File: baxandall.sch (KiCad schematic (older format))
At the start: 17 parts, among them P1 CONN_01X04, P3 CONN_01X03, U1 OP275

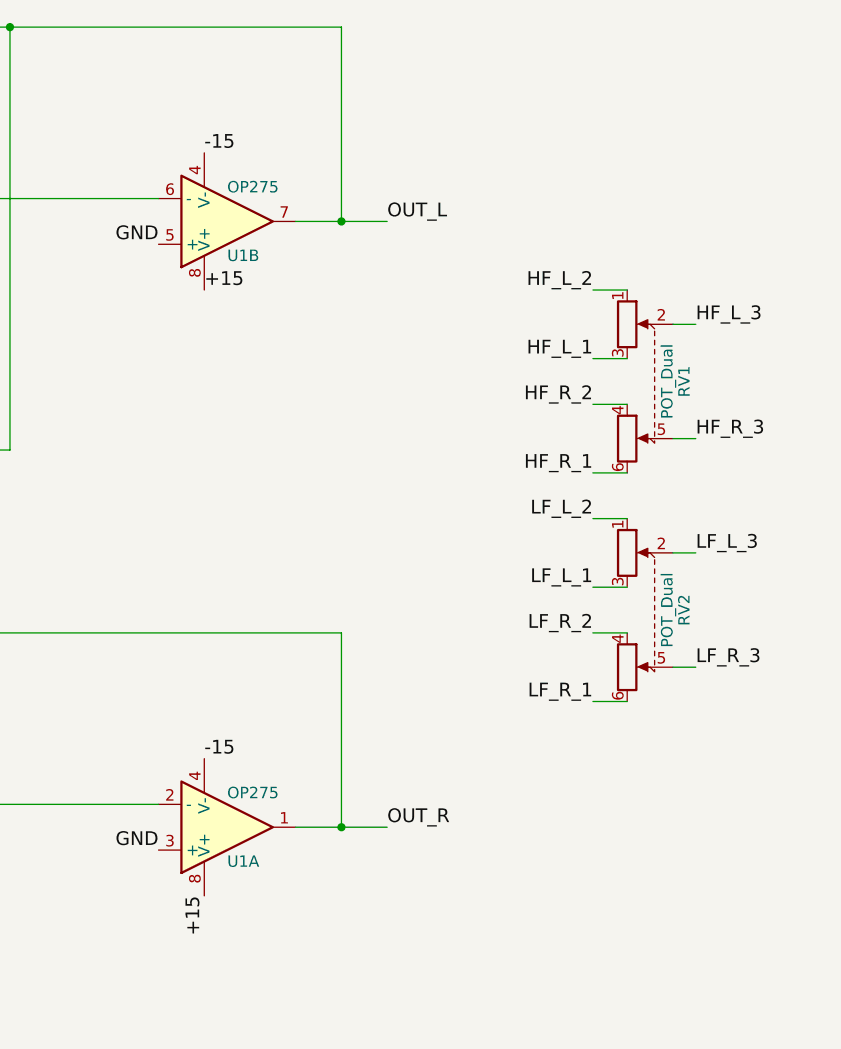
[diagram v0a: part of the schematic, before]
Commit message: Update potentiometers properties
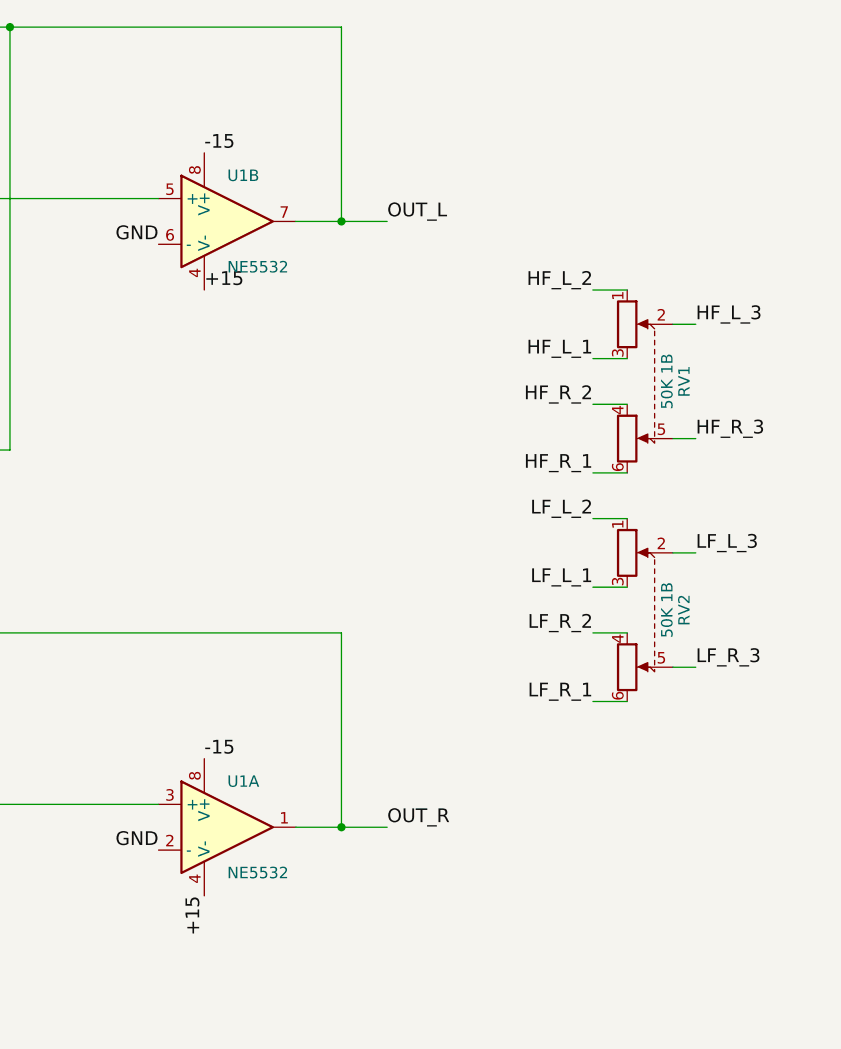
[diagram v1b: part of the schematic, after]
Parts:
- removed U1: OP275, Housings_DIP:DIP-8_W7.62mm_LongPads, symbol OP275
- added U1: NE5532, Housings_DIP:DIP-8_W7.62mm_LongPads, symbol NE5532
- RV1, RV2: value POT_Dual -> 50K 1B; Description (none) -> Potentiomètres 50 KOhms 20%; Distributor (none) -> Mouser; Distributor Part # (none) -> 688-RK09L122002M; Manufacturer (none) -> ALPS; Mfg_Part_# (none) -> RK09L122002M
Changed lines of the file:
@@
 LIBS:contrib
 LIBS:valves
+LIBS:baxandall-cache
 EELAYER 25 0
 EELAYER END
@@
 	1    3800 6350
 	0    1    1    0
-$EndComp
-$Comp
-L OP275 U1
-U 1 1 56A0BD66
-P 5050 5350
-F 0 "U1" H 5050 5500 50  0000 L CNN
-F 1 "OP275" H 5050 5200 50  0000 L CNN
-F 2 "Housings_DIP:DIP-8_W7.62mm_LongPads" H 4950 5400 50  0001 C CNN
-F 3 "" H 5050 5500 50  0000 C CNN
-	1    5050 5350
-	1    0    0    1
 $EndComp
 $Comp
@@
 Text Label 7150 1050 2    60   ~ 0
 GND
-$Comp
-L OP275 U1
-U 2 1 56AA63D5
-P 5050 2700
-F 0 "U1" H 5050 2850 50  0000 L CNN
-F 1 "OP275" H 5050 2550 50  0000 L CNN
-F 2 "Housings_DIP:DIP-8_W7.62mm_LongPads" H 4950 2750 50  0001 C CNN
-F 3 "" H 5050 2850 50  0000 C CNN
-	2    5050 2700
-	1    0    0    1
-$EndComp
 Text Label 4950 3000 0    60   ~ 0
 +15
@@
 P 6900 3400
 F 0 "RV1" H 6900 3550 50  0000 C CNN
-F 1 "POT_Dual" H 6900 3475 50  0000 C CNN
+F 1 "50K 1B" H 6900 3475 50  0000 C CNN
 F 2 "" H 7150 3325 50  0001 C CNN
-F 3 "" H 7150 3325 50  0001 C CNN
+F 3 "http://www.alps.com/prod/info/E/HTML/Potentiometer/RotaryPotentiometers/RK09L/RK09L122002M.html" H 7150 3325 50  0001 C CNN
+F 4 "RK09L122002M" H 6900 3400 60  0001 C CNN "Mfg_Part_#"
+F 5 "Mouser" H 6900 3400 60  0001 C CNN "Distributor"
+F 6 "688-RK09L122002M" H 6900 3400 60  0001 C CNN "Distributor Part #"
+F 7 "Potentiomètres 50 KOhms 20%" H 6900 3400 60  0001 C CNN "Description"
+F 8 "ALPS" H 6900 3400 60  0001 C CNN "Manufacturer"
 	1    6900 3400
 	0    1    1    0
@@
 Wire Wire Line
 	6650 3800 6800 3800
+Wire Wire Line
+	6650 4800 6800 4800
+Wire Wire Line
+	6800 4500 6650 4500
+Wire Wire Line
+	6650 4300 6800 4300
+Wire Wire Line
+	6800 4000 6650 4000
+Wire Wire Line
+	7000 4150 7100 4150
+Wire Wire Line
+	7100 4650 7000 4650
+$Comp
+L NE5532 U1
+U 2 1 5A0DA73B
+P 5050 2700
+F 0 "U1" H 5050 2900 50  0000 L CNN
+F 1 "NE5532" H 5050 2500 50  0000 L CNN
+F 2 "Housings_DIP:DIP-8_W7.62mm_LongPads" H 5050 2700 50  0001 C CNN
+F 3 "http://www.ti.com/lit/gpn/ne5532" H 5050 2700 50  0001 C CNN
+F 4 "NE5532P" H 5050 2700 60  0001 C CNN "Mfg_Part_#"
+F 5 "Mouser" H 5050 2700 60  0001 C CNN "Distributor"
+F 6 "595-NE5532P" H 5050 2700 60  0001 C CNN "Distributor Part #"
+F 7 "8-PDIP" H 5050 2700 60  0001 C CNN "Package"
+F 8 "Amplificateurs opérationnels - Amplis-Op Dual Low Noise" H 5050 2700 60  0001 C CNN "Description"
+F 9 "Texas Instruments" H 5050 2700 60  0001 C CNN "Manufacturer"
+	2    5050 2700
+	1    0    0    -1
+$EndComp
+$Comp
+L NE5532 U1
+U 1 1 5A0DAB29
+P 5050 5350
+F 0 "U1" H 5050 5550 50  0000 L CNN
+F 1 "NE5532" H 5050 5150 50  0000 L CNN
+F 2 "Housings_DIP:DIP-8_W7.62mm_LongPads" H 5050 5350 50  0001 C CNN
+F 3 "http://www.ti.com/lit/gpn/ne5532" H 5050 5350 50  0001 C CNN
+F 4 "NE5532P" H 5050 5350 60  0001 C CNN "Mfg_Part_#"
+F 5 "Mouser" H 5050 5350 60  0001 C CNN "Distributor"
+F 6 "595-NE5532P" H 5050 5350 60  0001 C CNN "Distributor Part #"
+F 7 "8-PDIP" H 5050 5350 60  0001 C CNN "Package"
+F 8 "Amplificateurs opérationnels - Amplis-Op Dual Low Noise" H 5050 5350 60  0001 C CNN "Description"
+F 9 "Texas Instruments" H 5050 5350 60  0001 C CNN "Manufacturer"
+	1    5050 5350
+	1    0    0    -1
+$EndComp
 $Comp
 L POT_Dual RV2
-U 1 1 5A0C7786
+U 1 1 5A0DB04F
 P 6900 4400
 F 0 "RV2" H 6900 4550 50  0000 C CNN
-F 1 "POT_Dual" H 6900 4475 50  0000 C CNN
+F 1 "50K 1B" H 6900 4475 50  0000 C CNN
 F 2 "" H 7150 4325 50  0001 C CNN
-F 3 "" H 7150 4325 50  0001 C CNN
+F 3 "http://www.alps.com/prod/info/E/HTML/Potentiometer/RotaryPotentiometers/RK09L/RK09L122002M.html" H 7150 4325 50  0001 C CNN
+F 4 "RK09L122002M" H 6900 4400 60  0001 C CNN "Mfg_Part_#"
+F 5 "Mouser" H 6900 4400 60  0001 C CNN "Distributor"
+F 6 "688-RK09L122002M" H 6900 4400 60  0001 C CNN "Distributor Part #"
+F 7 "Potentiomètres 50 KOhms 20%" H 6900 4400 60  0001 C CNN "Description"
+F 8 "ALPS" H 6900 4400 60  0001 C CNN "Manufacturer"
 	1    6900 4400
 	0    1    1    0
 $EndComp
-Wire Wire Line
-	6650 4800 6800 4800
-Wire Wire Line
-	6800 4500 6650 4500
-Wire Wire Line
-	6650 4300 6800 4300
-Wire Wire Line
-	6800 4000 6650 4000
-Wire Wire Line
-	7000 4150 7100 4150
-Wire Wire Line
-	7100 4650 7000 4650
 $EndSCHEMATC

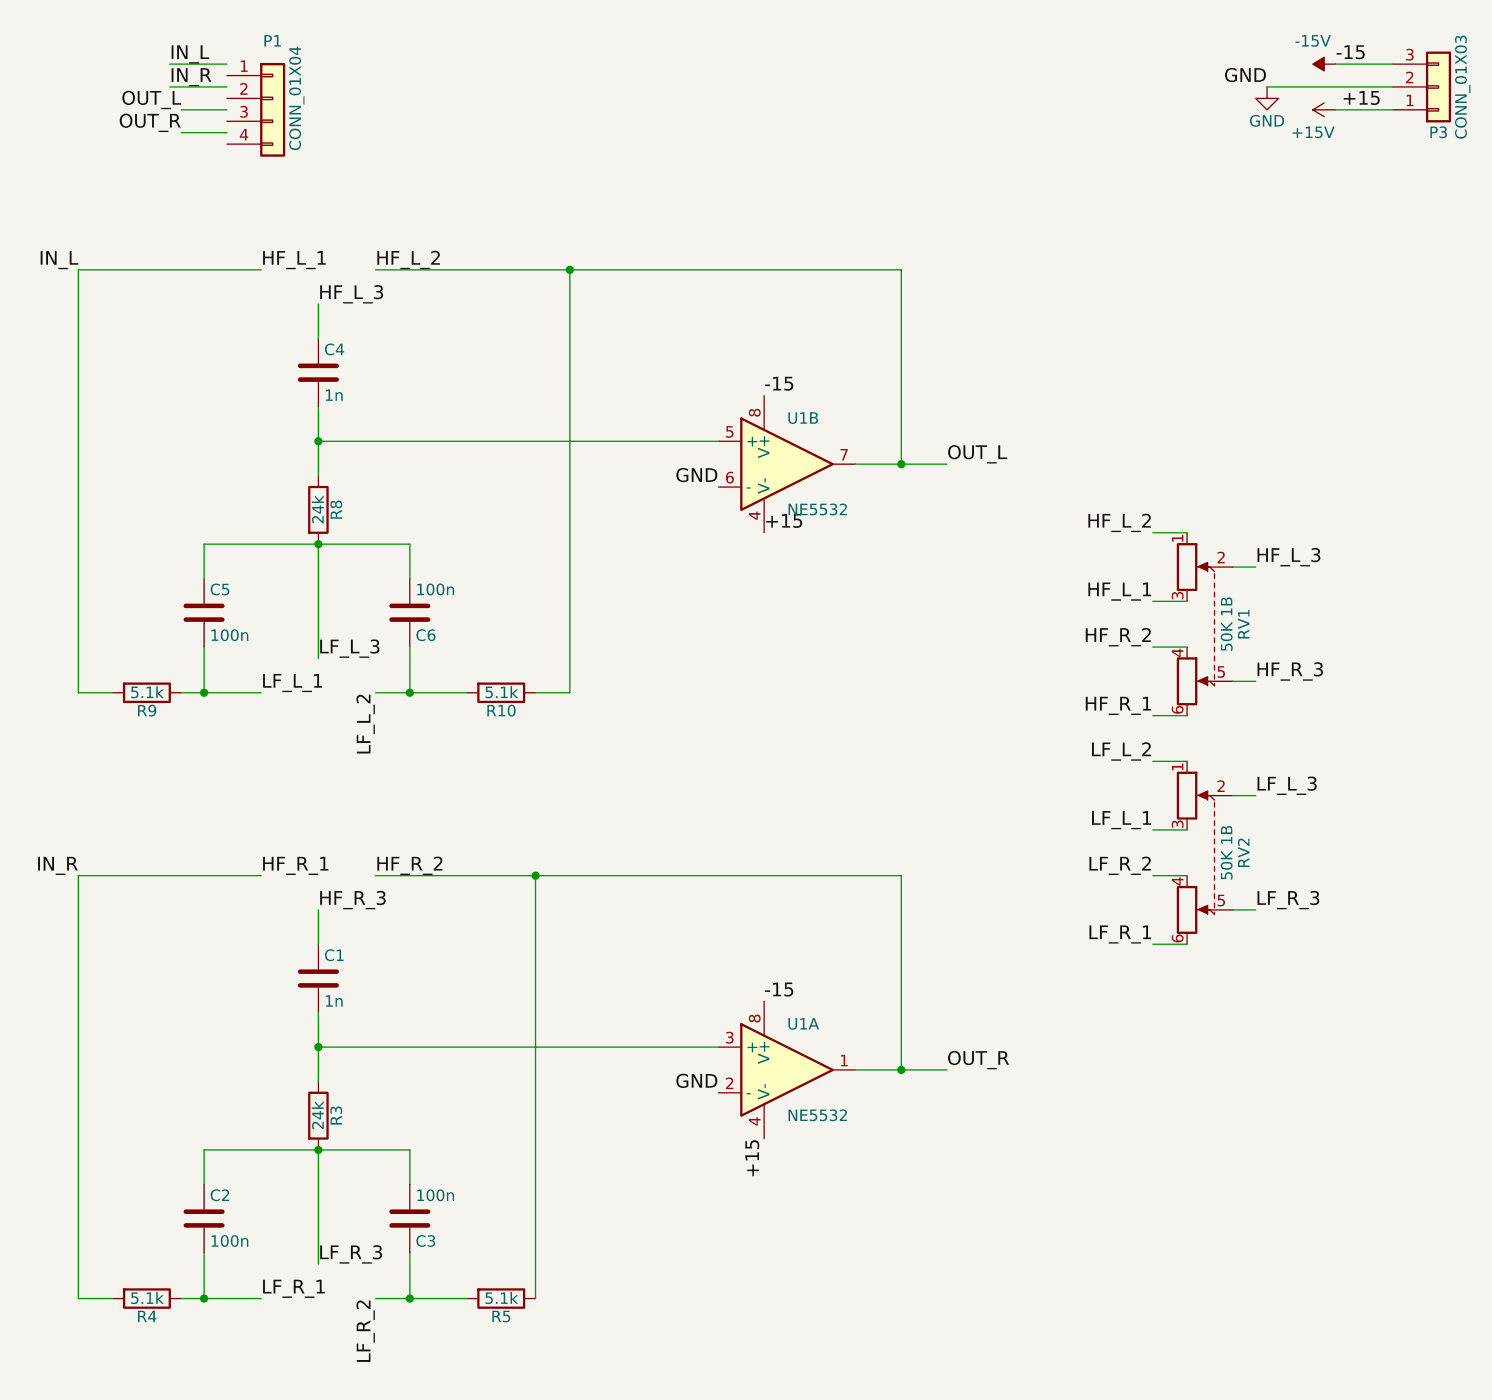
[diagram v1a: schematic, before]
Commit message: update components references and footprints
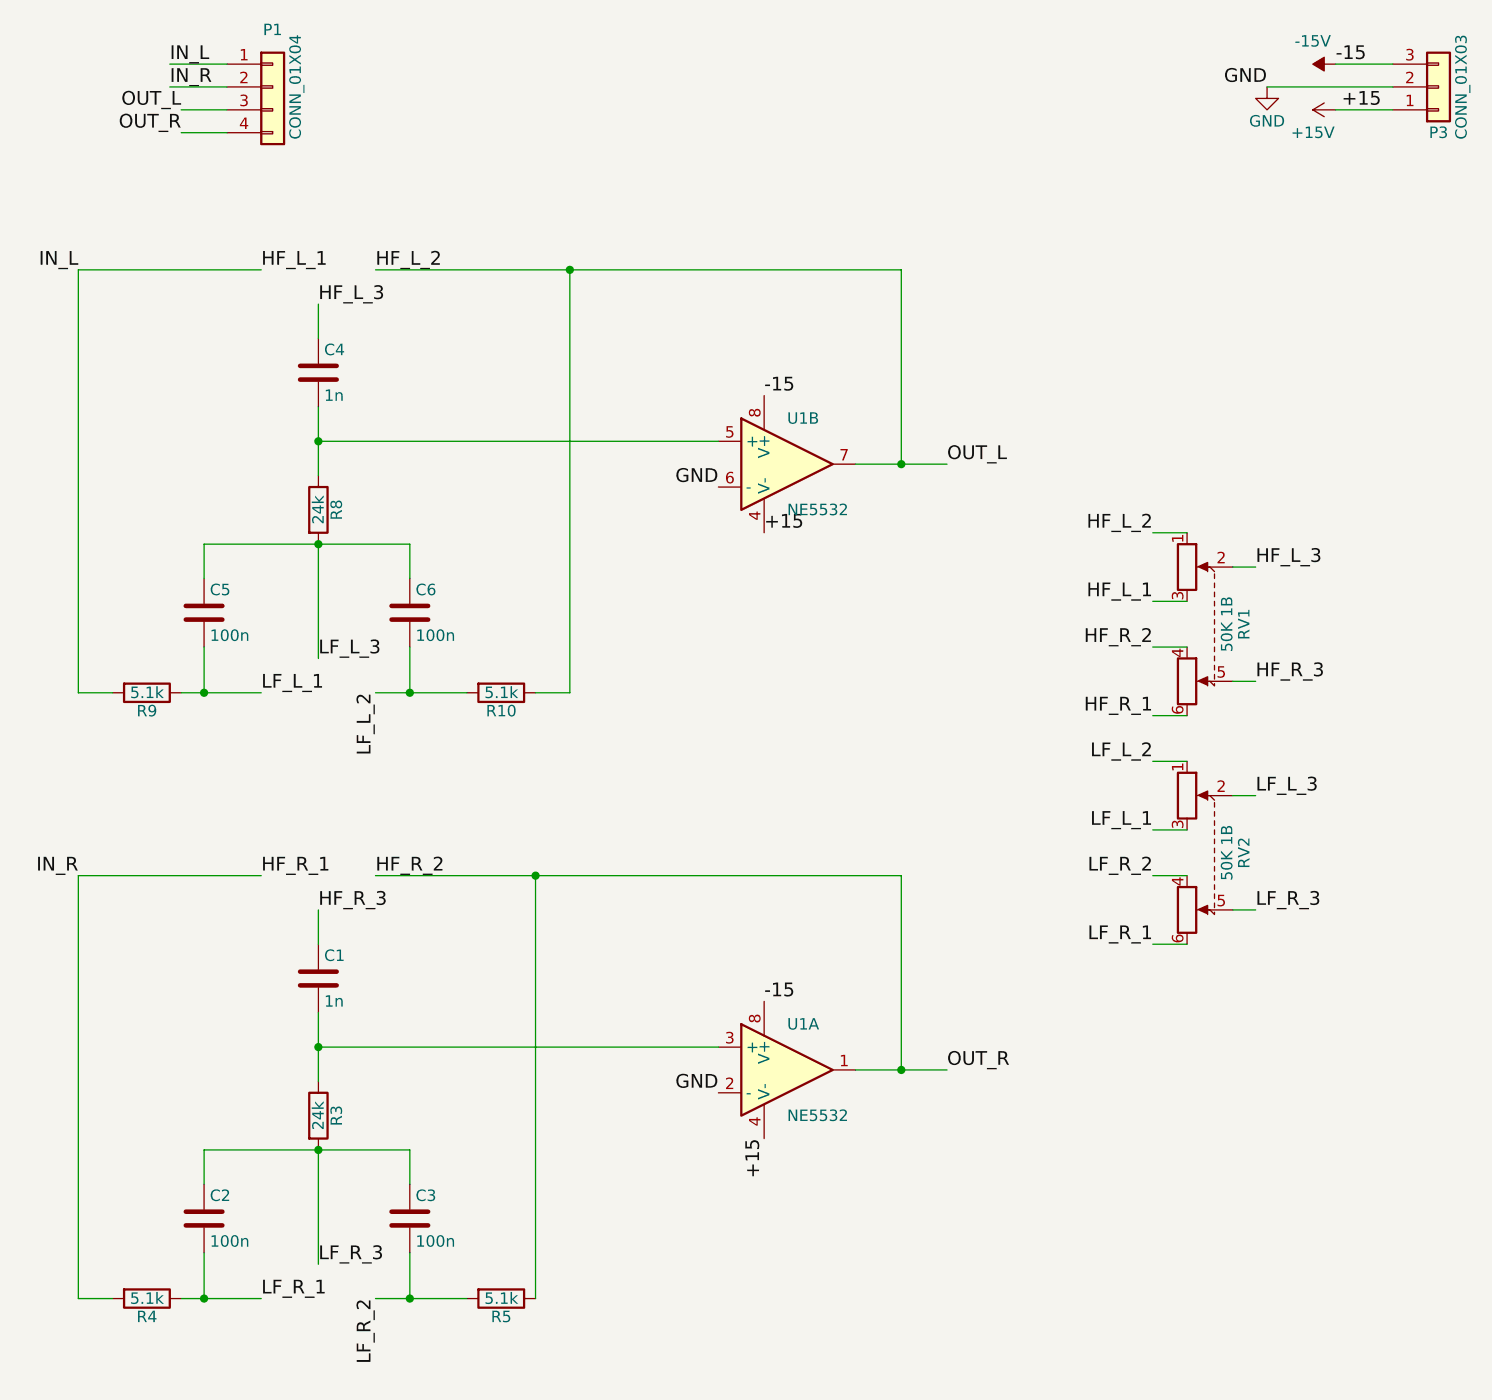
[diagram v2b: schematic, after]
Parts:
- C1, C4: footprint Capacitors_ThroughHole:C_Disc_D6_P5 -> Capacitors_THT:C_Rect_L7.2mm_W5.5mm_P5.00mm_FKS2_FKP2_MKS2_MKP2; Description (none) -> Condensateurs à film 50volts 1000pF 5% LS 5mm; Distributor (none) -> Mouser; Distributor Part # (none) -> 80-MMK5102J50J01L4; Manufacturer (none) -> Kemet; Mfg_Part_# (none) -> MMK5102J50J01L4BULK; Package (none) -> 2-THT
- C2, C3, C5, C6: Description (none) -> Condensateurs à film 50volts 0.1uF 10% LS 5mm; Distributor (none) -> Mouser; Distributor Part # (none) -> 80-MMK5104K50J01L4; Manufacturer (none) -> Kemet; Mfg_Part_# (none) -> MMK5104K50J01L4BULK; Package (none) -> 2-THT
- R10, R4, R5, R9: footprint Resistors_ThroughHole:Resistor_Horizontal_RM15mm -> Resistors_THT:R_Axial_DIN0204_L3.6mm_D1.6mm_P5.08mm_Horizontal; Description (none) -> Résistances à couche mince - Trou traversant .4watt 5.1Kohm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; Distributor (none) -> Mouser; Distributor Part # (none) -> 594-5063JD5K100F; Manufacturer (none) -> Vishay / Beyschlag; Mfg_Part_# (none) -> MBA02040C5101FC100; Package (none) -> 2-THT
- R3, R8: footprint Resistors_ThroughHole:Resistor_Horizontal_RM15mm -> Resistors_THT:R_Axial_DIN0204_L3.6mm_D1.6mm_P5.08mm_Horizontal; Description (none) -> Résistances à couche mince - Trou traversant .4watt 24Kohms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; Distributor (none) -> Mouser; Distributor Part # (none) -> 594-5063JD24K00F; Manufacturer (none) -> Vishay / Beyschlag; Mfg_Part_# (none) -> MBA02040C2402FC100; Package (none) -> 2-THT
- RV1, RV2: footprint (none) -> potentiometers:Potentiometer_ALPS_RK09
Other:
- moved on the sheet: P1

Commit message: Add headers references
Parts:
- P1: Description (none) -> Embases et logements de câbles WR-PHD 2.54mm Hdr 4P Single 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; Distributor (none) -> Mouser; Distributor Part # (none) -> 710-61300411021; Manufacturer (none) -> Wurth Electronics; Mfg_Part_# (none) -> 61300411021; Package (none) -> 4-THT
- P3: Description (none) -> Embases et logements de câbles WR-PHD 2.54mm Hdr 3P Single 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; Distributor (none) -> Mouser; Distributor Part # (none) -> 710-61300311021; Manufacturer (none) -> Wurth Electronics; Mfg_Part_# (none) -> 61300311021; Package (none) -> 3-THT
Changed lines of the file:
@@
 F 1 "CONN_01X03" V 8000 1050 50  0000 C CNN
 F 2 "Pin_Headers:Pin_Header_Angled_1x03" H 7900 1050 50  0001 C CNN
-F 3 "" H 7900 1050 50  0000 C CNN
+F 3 "http://www.mouser.com/ds/2/445/6130xx11021-538004.pdf" H 7900 1050 50  0001 C CNN
+F 4 "61300311021" H 7900 1050 60  0001 C CNN "Mfg_Part_#"
+F 5 "Mouser" H 7900 1050 60  0001 C CNN "Distributor"
+F 6 "710-61300311021" H 7900 1050 60  0001 C CNN "Distributor Part #"
+F 7 "3-THT" H 7900 1050 60  0001 C CNN "Package"
+F 8 "Embases et logements de câbles WR-PHD 2.54mm Hdr 3P Single RA Gold" H 7900 1050 60  0001 C CNN "Description"
+F 9 "Wurth Electronics" H 7900 1050 60  0001 C CNN "Manufacturer"
 	1    7900 1050
 	1    0    0    1
@@
 F 1 "CONN_01X04" V 2900 1050 50  0000 C CNN
 F 2 "Pin_Headers:Pin_Header_Angled_1x04" H 2800 1050 50  0001 C CNN
-F 3 "" H 2800 1050 50  0000 C CNN
+F 3 "http://www.mouser.com/ds/2/445/6130xx11021-538004.pdf" H 2800 1050 50  0001 C CNN
+F 4 "61300411021" H 2800 1050 60  0001 C CNN "Mfg_Part_#"
+F 5 "Mouser" H 2800 1050 60  0001 C CNN "Distributor"
+F 6 "710-61300411021" H 2800 1050 60  0001 C CNN "Distributor Part #"
+F 7 "4-THT" H 2800 1050 60  0001 C CNN "Package"
+F 8 "Embases et logements de câbles WR-PHD 2.54mm Hdr 4P Single RA Gold" H 2800 1050 60  0001 C CNN "Description"
+F 9 "Wurth Electronics" H 2800 1050 60  0001 C CNN "Manufacturer"
 	1    2800 1050
 	1    0    0    -1
